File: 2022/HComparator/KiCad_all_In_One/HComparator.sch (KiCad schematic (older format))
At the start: 22 parts, among them M1 PMOS_OR1, M10 NMOS_OR1, M11 NMOS_OR1, M12 PMOS_OR1, M13 NMOS_OR1, M14 NMOS_OR1, M15 PMOS_OR1, M16 NMOS_OR1, M17 PMOS_OR1, M18 NMOS_OR1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

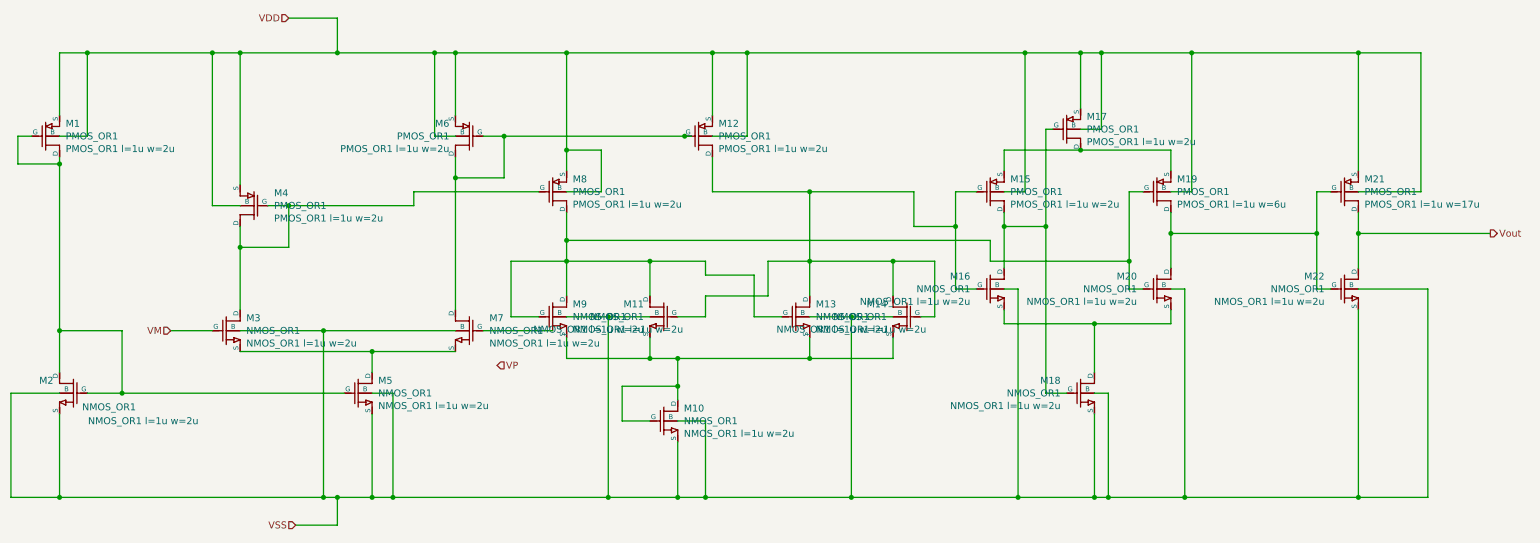
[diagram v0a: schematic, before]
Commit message: テストベンチを通し、シミュレーション結果も得た。 さらに、再度 LVS を確認した。
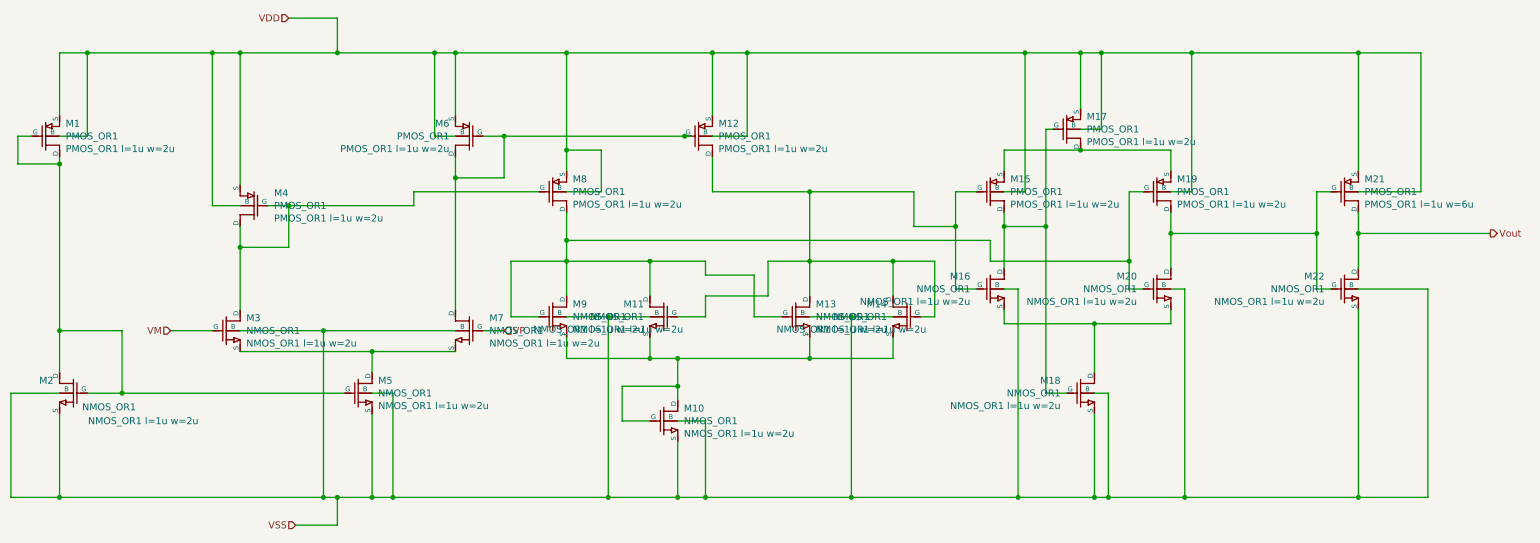
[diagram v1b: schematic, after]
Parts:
- M19: Spice_Model PMOS_OR1 l=1u w=6u -> PMOS_OR1 l=1u w=2u
- M21: Spice_Model PMOS_OR1 l=1u w=17u -> PMOS_OR1 l=1u w=6u
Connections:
- net VP: now also M7.2 (G)
